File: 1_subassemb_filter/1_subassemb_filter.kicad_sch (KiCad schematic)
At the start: 9 parts

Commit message: Updates to the filter
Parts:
- C2: value 0.2 u -> 10 u
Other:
- note added: "Decoupling"
- moved on the sheet: BAR1, C1, C2, R1, R2, R3, R4, R5, R6

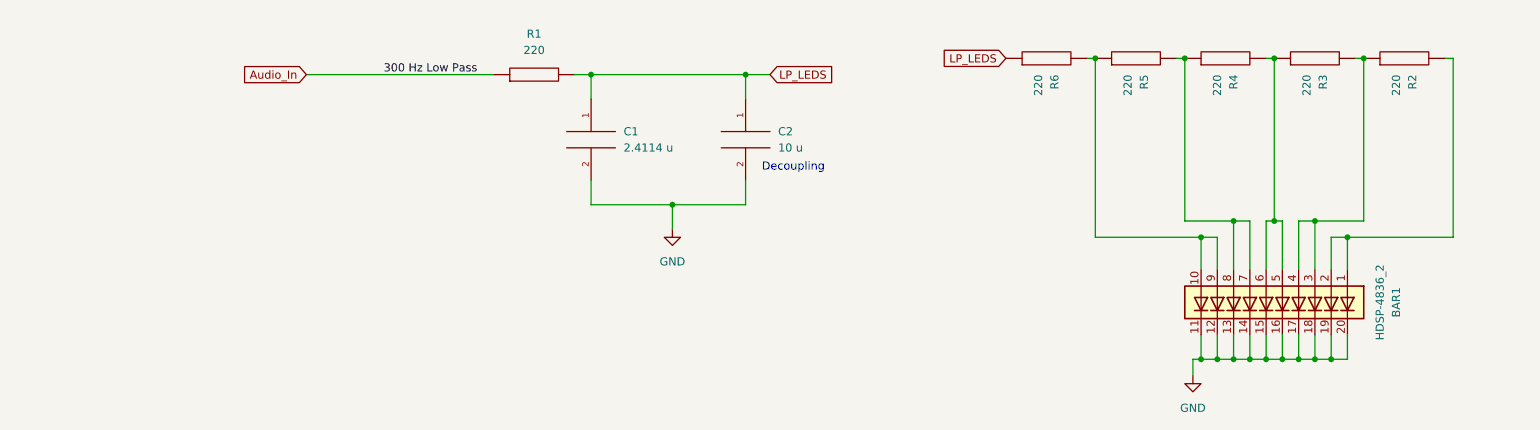
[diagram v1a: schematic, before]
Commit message: An actually working LP Filter with a hopefully working comparator system for the LEDs.
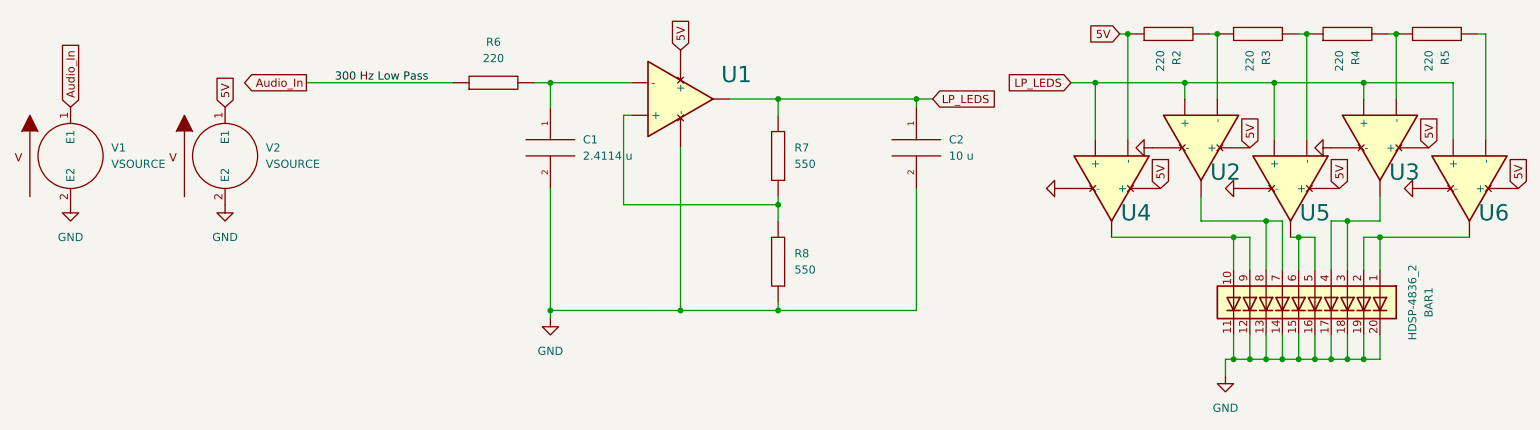
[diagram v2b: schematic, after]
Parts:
- removed R6: 220, symbol pspice:R
- added R7, R8: 550, symbol pspice:R
- added U1, U2, U3, U4, U5, U6: X-opamp,IEEE, symbol Generic:X-opamp,IEEE
- added V1, V2: VSOURCE, symbol pspice:VSOURCE
- BAR1: Spice_Model (none) -> HDSP-4836_2; Spice_Netlist_Enabled (none) -> N; Spice_Primitive (none) -> R
- renumbered R5 to R2, R4 to R3, R3 to R4, R2 to R5, R1 to R6
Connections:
- net Audio_In: now also V1.1 (E1)
- net GND: now also R8.1, U1.4 (-), U2.4 (-), U3.4 (-), U4.4 (-), U5.4 (-), U6.4 (-), V1.2 (E2), V2.2 (E2)
- net LP_LEDS: now also R7.2, U1.5 (OUT), U2.1 (+), U3.1 (+), U4.1 (+), U5.1 (+), U6.1 (+); no longer C1.1, R6.2
- net at R3.2, R4.1: now also U5.2 (-); no longer BAR1.5 (A), BAR1.6 (A)
- net at R4.2, R5.1: now also U3.2 (-); no longer BAR1.3 (A), BAR1.4 (A)
- net at BAR1.10 (A), BAR1.9 (A): now also U4.5 (OUT); no longer R2.1
- net at R2.2, R3.1: now also U2.2 (-); no longer BAR1.7 (A), BAR1.8 (A)
- net at BAR1.1 (A), BAR1.2 (A): now also U6.5 (OUT); no longer R5.2
- new net: R7.1, R8.2, U1.1 (+)
- new net: BAR1.3 (A), BAR1.4 (A), U3.5 (OUT)
- new net: BAR1.5 (A), BAR1.6 (A), U5.5 (OUT)
- new net: BAR1.7 (A), BAR1.8 (A), U2.5 (OUT)
- new net: C1.1, R6.2, U1.2 (-)
- new net: R5.2, U6.2 (-)
- new net 5V: R2.1, U1.3 (+), U2.3 (+), U3.3 (+), U4.2 (-), U4.3 (+), U5.3 (+), U6.3 (+), V2.1 (E1)
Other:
- note removed: "Decoupling"
- moved on the sheet: BAR1, C1, R2, R3, R4, R5, R6

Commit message: Fully functional LP Filter and Comparator-Resistor net with the LEDs
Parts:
- added C3: 4.7 u, symbol pspice:C
- added R6: 220, symbol pspice:R
- added R9: 550, symbol pspice:R
- added U2: X-opamp,IEEE, symbol Generic:X-opamp,IEEE
- C1: value 2.4114 u -> 4.7 u
- C2: value 10 u -> 100 u
- R7: value 550 -> 220
- R8: value 550 -> 5500
- V1: Spice_Model dc 0 ac 5 0 sin(0 2 100) -> dc 0 ac 5 0 sin(0 0.5 700)
- renumbered R2 to R1, R3 to R2, R4 to R3, R5 to R4, R6 to R5, U2 to U3, U3 to U4, U4 to U5, U5 to U6, U6 to U7
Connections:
- net 5V: now also U2.3 (+)
- net GND: now also C3.2, R6.1, R9.1, U2.4 (-); no longer C1.2, R8.1
- net LP_LEDS: now also R8.2, U2.5 (OUT); no longer C2.1, R7.2, U1.5 (OUT)
- net at C1.1, R5.2: now also U1.1 (+); no longer U1.2 (-)
- net at R4.2, U7.2 (-): now also R6.2
- new net: C2.1, R7.2, U2.1 (+)
- new net: C1.2, C3.1
- new net: R8.1, R9.2, U2.2 (-)
- new net LP Pre-LP: R7.1, U1.2 (-), U1.5 (OUT)
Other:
- note added: "2.35uF total (2.4114uF is ideal)"
- note added: "300 Hz Low-Pass"
- moved on the sheet: BAR1, C1, R1, R2, R3, R4, R5, U1, U3, U4, U5, U6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

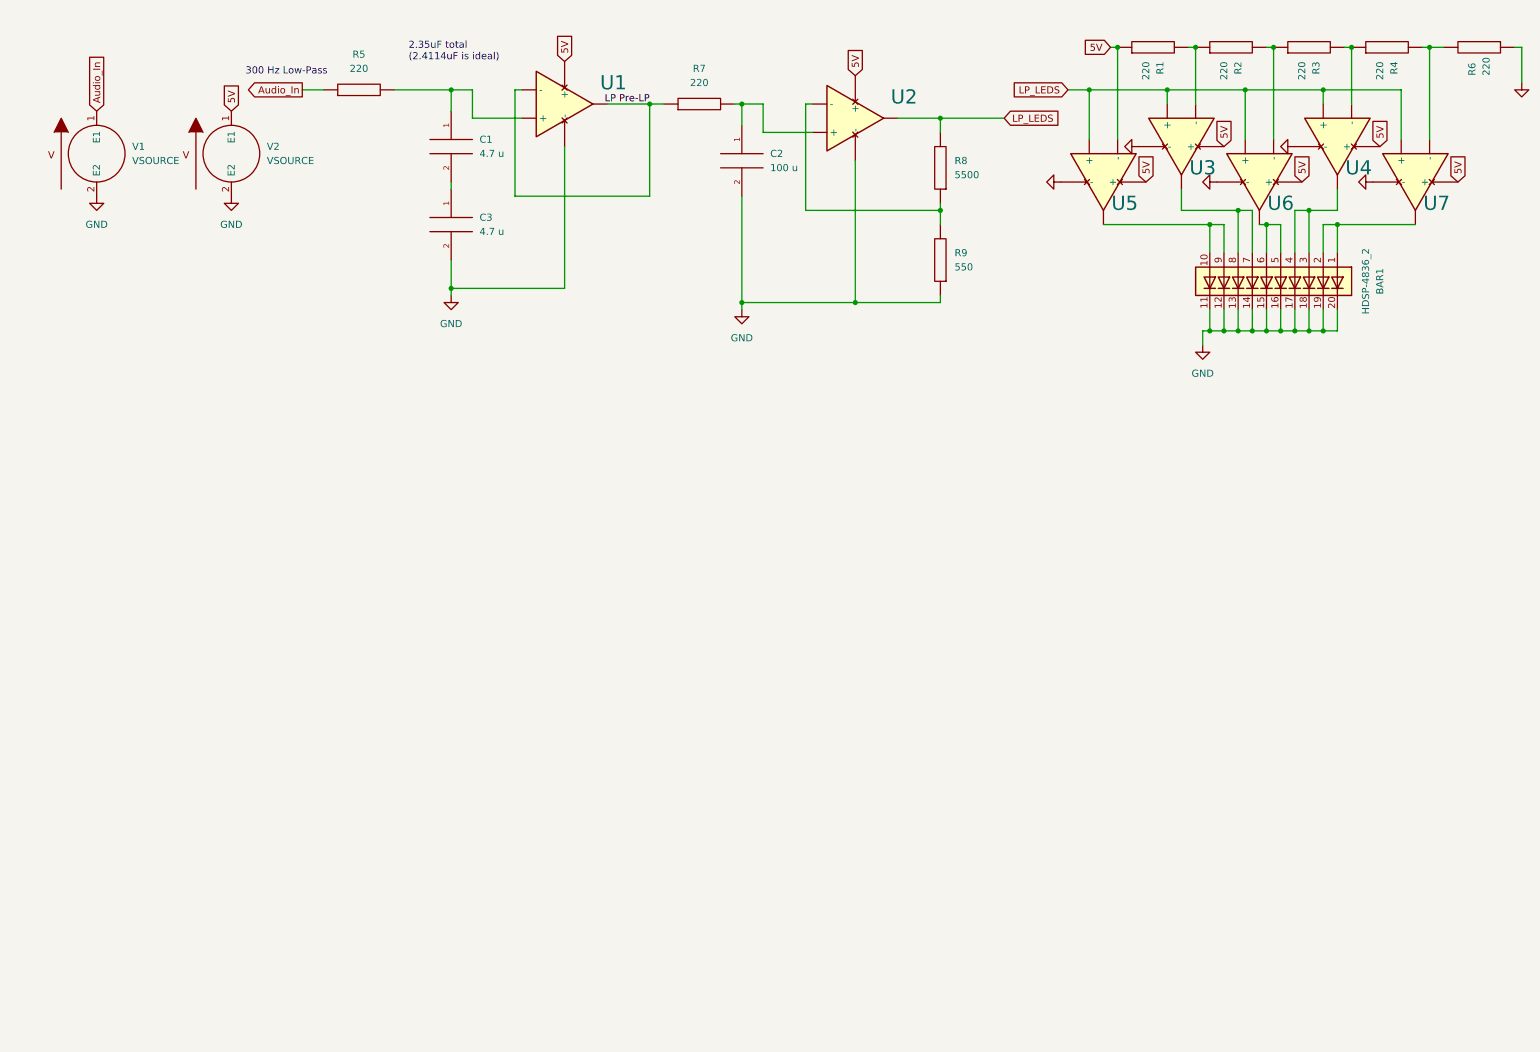
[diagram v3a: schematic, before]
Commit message: Added high-pass filter and made the whole system a bit more modular
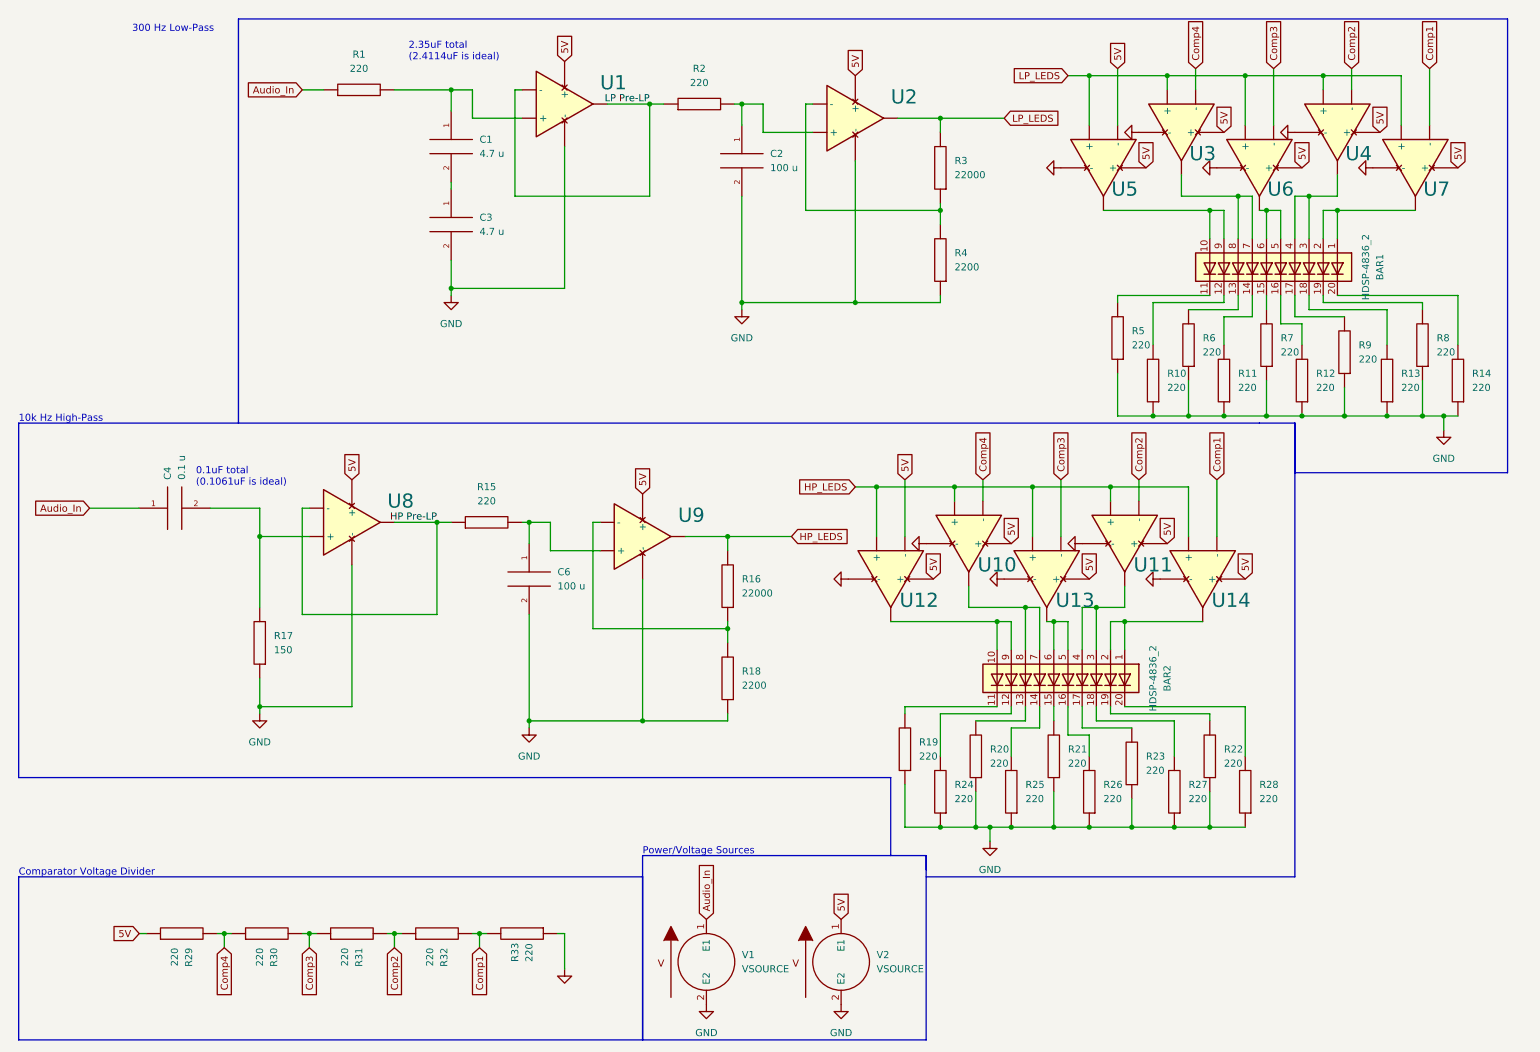
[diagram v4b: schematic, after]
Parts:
- removed R1, R2, R3, R4: 220, symbol pspice:R
- added BAR2: HDSP-4836_2, Display:HDSP-4836, symbol LED:HDSP-4836_2
- added C4: 0.1 u, symbol pspice:C
- added C6: 100 u, symbol pspice:C
- added R10, R11, R12, R13, R14, R15, R19, R20, R21, R22, R23, R24, R25, R26, R27, R28, R29, R30, R31, R32, R33, R5, R7, R8, R9: 220, symbol pspice:R
- added R16: 22000, symbol pspice:R
- added R17: 150, symbol pspice:R
- added R18: 2200, symbol pspice:R
- added U10, U11, U12, U13, U14, U8, U9: X-opamp,IEEE, symbol Generic:X-opamp,IEEE
- R3: renamed from R8; value 5500 -> 22000
- R4: renamed from R9; value 550 -> 2200
- V1: Spice_Model dc 0 ac 5 0 sin(0 0.5 700) -> dc 0 ac 5 0 sin(0 1.5 10k)
- renumbered R5 to R1, R7 to R2
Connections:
- net 5V: now also R29.1, U10.3 (+), U11.3 (+), U12.2 (-), U12.3 (+), U13.3 (+), U14.3 (+), U8.3 (+), U9.3 (+)
- net Audio_In: now also C4.1
- net GND: now also C6.2, R10.1, R11.1, R12.1, R13.1, R14.1, R17.1, R18.1, R19.1, R20.1, R21.1, R22.1, R23.1, R24.1, R25.1, R26.1, R27.1, R28.1, R33.1, R5.1, R7.1, R8.1, R9.1, U10.4 (-), U11.4 (-), U12.4 (-), U13.4 (-), U14.4 (-), U8.4 (-), U9.4 (-); no longer BAR1.11 (K), BAR1.12 (K), BAR1.13 (K), BAR1.14 (K), BAR1.15 (K), BAR1.16 (K), BAR1.17 (K), BAR1.18 (K), BAR1.19 (K), BAR1.20 (K)
- net at R6.2: now also BAR1.13 (K); no longer U7.2 (-)
- net Comp3: now reaches U6.2 (-)
- net Comp3: now also R30.2, R31.1, U13.2 (-)
- net Comp2: now reaches U4.2 (-)
- net Comp2: now also R31.2, R32.1, U11.2 (-)
- net Comp4: now reaches U3.2 (-)
- net Comp4: now also R29.2, R30.1, U10.2 (-)
- new net: BAR2.1 (A), BAR2.2 (A), U14.5 (OUT)
- new net: BAR2.10 (A), BAR2.9 (A), U12.5 (OUT)
- new net: BAR2.11 (K), R19.2
- new net: BAR2.12 (K), R24.2
- new net: BAR2.13 (K), R20.2
- new net: BAR2.14 (K), R25.2
- new net: BAR2.15 (K), R21.2
- new net: BAR2.16 (K), R26.2
- new net: BAR2.17 (K), R23.2
- new net: BAR2.18 (K), R27.2
- new net: BAR2.19 (K), R22.2
- new net: BAR2.20 (K), R28.2
- new net: BAR2.3 (A), BAR2.4 (A), U11.5 (OUT)
- new net: BAR2.5 (A), BAR2.6 (A), U13.5 (OUT)
- new net: BAR2.7 (A), BAR2.8 (A), U10.5 (OUT)
- new net: C4.2, R17.2, U8.1 (+)
- new net: BAR1.17 (K), R9.2
- new net: BAR1.19 (K), R8.2
- new net: R16.1, R18.2, U9.2 (-)
- new net: BAR1.11 (K), R5.2
- new net: BAR1.12 (K), R10.2
- new net: BAR1.14 (K), R11.2
- new net: BAR1.15 (K), R7.2
- new net: BAR1.16 (K), R12.2
- new net: BAR1.18 (K), R13.2
- new net: BAR1.20 (K), R14.2
- new net: C6.1, R15.2, U9.1 (+)
- new net Comp1: R32.2, R33.2, U14.2 (-), U7.2 (-)
- new net HP Pre-LP: R15.1, U8.2 (-), U8.5 (OUT)
- new net HP_LEDS: R16.2, U10.1 (+), U11.1 (+), U12.1 (+), U13.1 (+), U14.1 (+), U9.5 (OUT)
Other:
- note added: "0.1uF total (0.1061uF is ideal)"
- note added: "10k Hz High-Pass"
- note added: "Comparator Voltage Divider"
- note added: "Power/Voltage Sources"
- moved on the sheet: BAR1, U3, U4, U5, U6, U7, V1, V2

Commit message: Low and high filter systems now ready
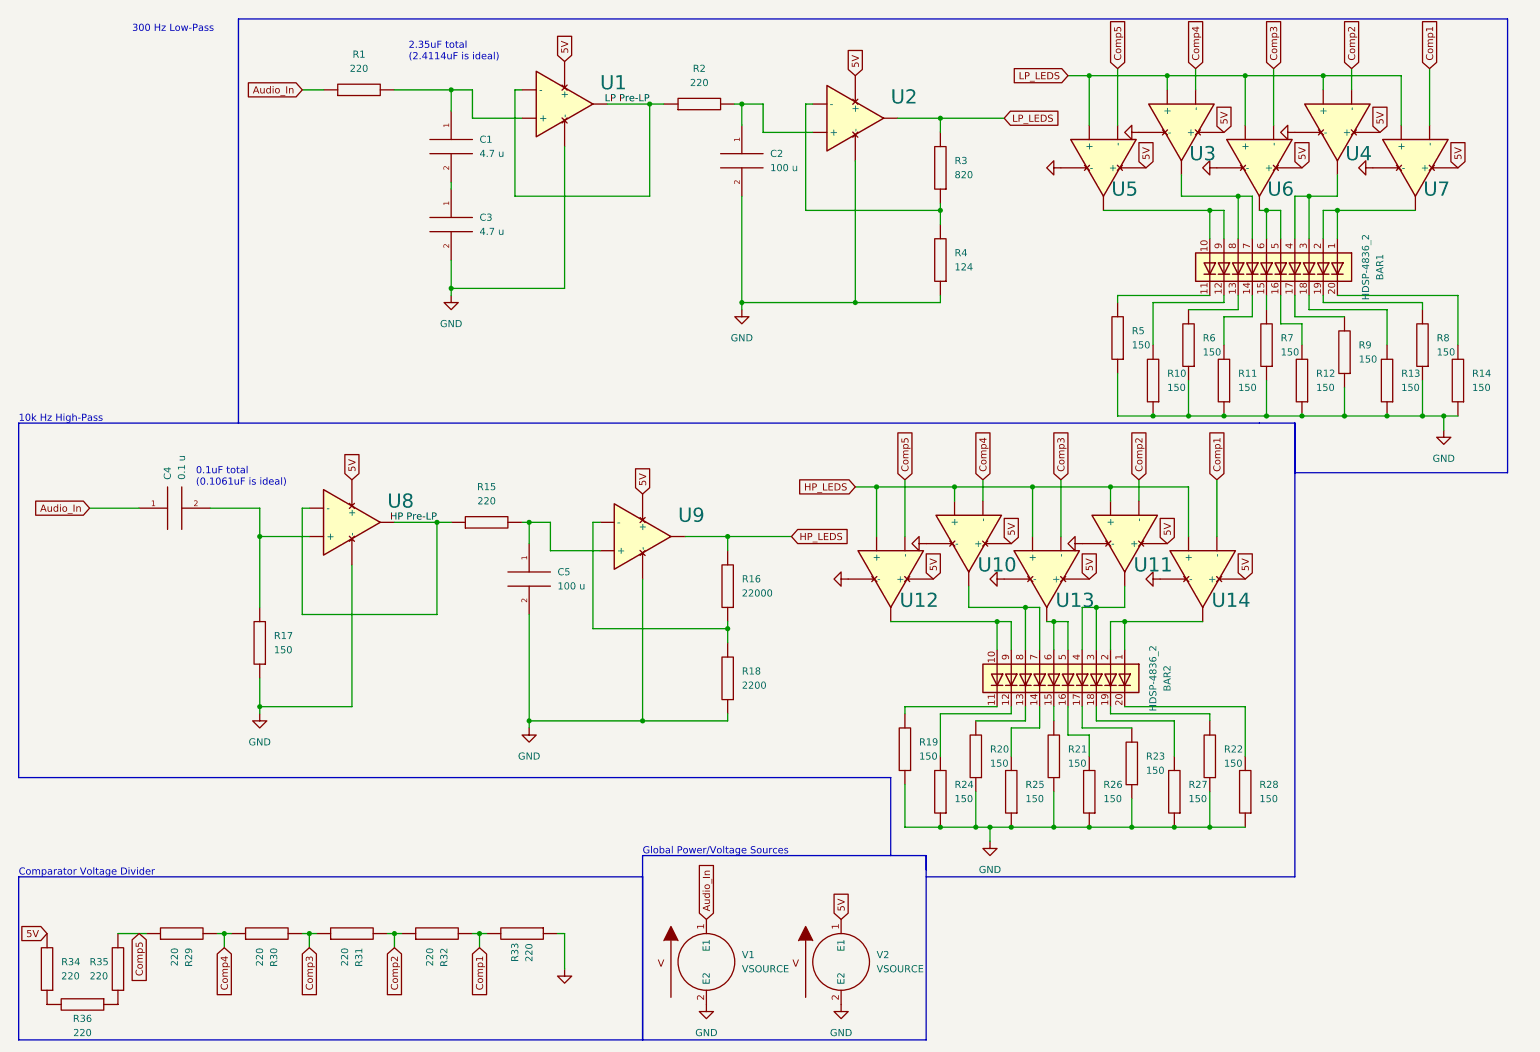
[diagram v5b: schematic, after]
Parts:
- added R34, R35, R36: 220, symbol pspice:R
- R10, R11, R12, R13, R14, R19, R20, R21, R22, R23, R24, R25, R26, R27, R28, R5, R6, R7, R8, R9: value 220 -> 150
- R3: value 22000 -> 820
- R4: value 2200 -> 124
- renumbered C6 to C5
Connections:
- net 5V: now also R34.2; no longer R29.1, U12.2 (-), U5.2 (-)
- new net: R34.1, R36.2
- new net: R35.1, R36.1
- new net Comp5: R29.1, R35.2, U12.2 (-), U5.2 (-)
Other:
- note added: "Global Power/Voltage Sources"
- note removed: "Power/Voltage Sources"
- title: (none) -> Low/High-Pass Filters with Bar Graph LEDs
